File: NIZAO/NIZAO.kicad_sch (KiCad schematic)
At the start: 6 parts, among them J1 Screw_Terminal_01x09, J2 Screw_Terminal_01x09, J3 Screw_Terminal_01x09, J4 Screw_Terminal_01x09

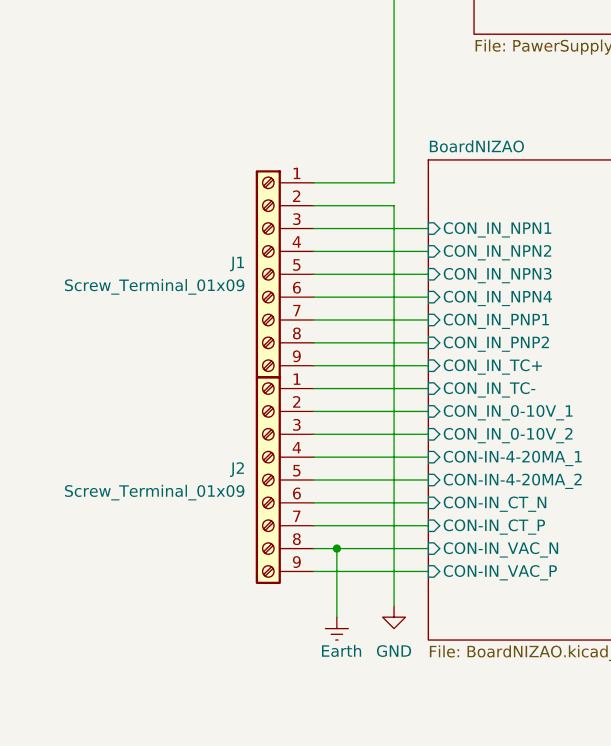
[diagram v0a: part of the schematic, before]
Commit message: Colocandos los 3d de los componetes en la placa NIZAO
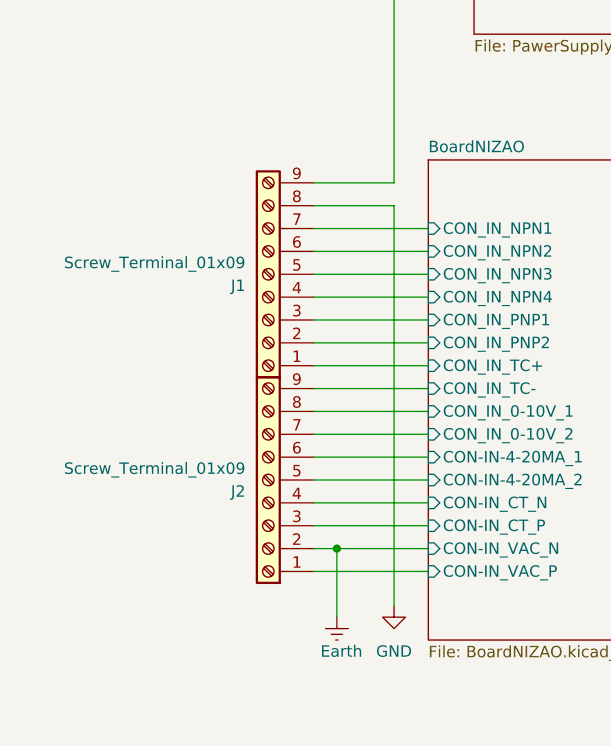
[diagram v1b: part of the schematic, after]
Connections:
- net +24V: now also J1.9 (Pin_9); no longer J1.1 (Pin_1)
- net BoardNIZAO/CON-IN-4-20MA_1: now also J2.6 (Pin_6); no longer J2.4 (Pin_4)
- net BoardNIZAO/CON-IN_CT_N: now also J2.4 (Pin_4); no longer J2.6 (Pin_6)
- net BoardNIZAO/CON-IN_CT_P: now also J2.3 (Pin_3); no longer J2.7 (Pin_7)
- net BoardNIZAO/CON-IN_VAC_P: now also J2.1 (Pin_1); no longer J2.9 (Pin_9)
- net BoardNIZAO/CON_IN_0-10V_1: now also J2.8 (Pin_8); no longer J2.2 (Pin_2)
- net BoardNIZAO/CON_IN_0-10V_2: now also J2.7 (Pin_7); no longer J2.3 (Pin_3)
- net BoardNIZAO/CON_IN_NPN1: now also J1.7 (Pin_7); no longer J1.3 (Pin_3)
- net BoardNIZAO/CON_IN_NPN2: now also J1.6 (Pin_6); no longer J1.4 (Pin_4)
- net BoardNIZAO/CON_IN_NPN4: now also J1.4 (Pin_4); no longer J1.6 (Pin_6)
- net BoardNIZAO/CON_IN_PNP1: now also J1.3 (Pin_3); no longer J1.7 (Pin_7)
- net BoardNIZAO/CON_IN_PNP2: now also J1.2 (Pin_2); no longer J1.8 (Pin_8)
- net BoardNIZAO/CON_IN_TC+: now also J1.1 (Pin_1); no longer J1.9 (Pin_9)
- net BoardNIZAO/CON_IN_TC-: now also J2.9 (Pin_9); no longer J2.1 (Pin_1)
- net Earth: now also J2.2 (Pin_2); no longer J2.8 (Pin_8)
- net GND: now also J1.8 (Pin_8); no longer J1.2 (Pin_2)
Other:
- moved on the sheet: J1, J2
